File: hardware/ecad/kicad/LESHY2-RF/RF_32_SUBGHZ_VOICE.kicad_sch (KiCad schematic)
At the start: 0 parts

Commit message: complete exact H2.3.1 RF power hierarchy
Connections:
- no-connect marks 0 -> 29

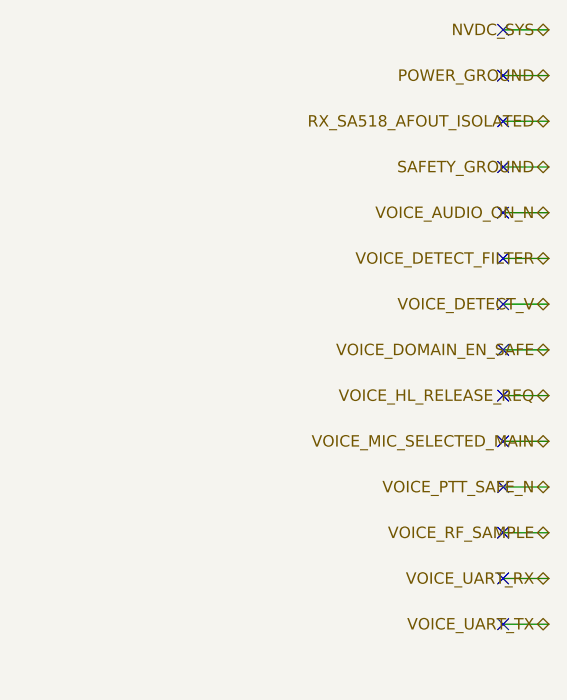
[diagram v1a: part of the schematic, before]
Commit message: complete exact H2.3.4 power rails
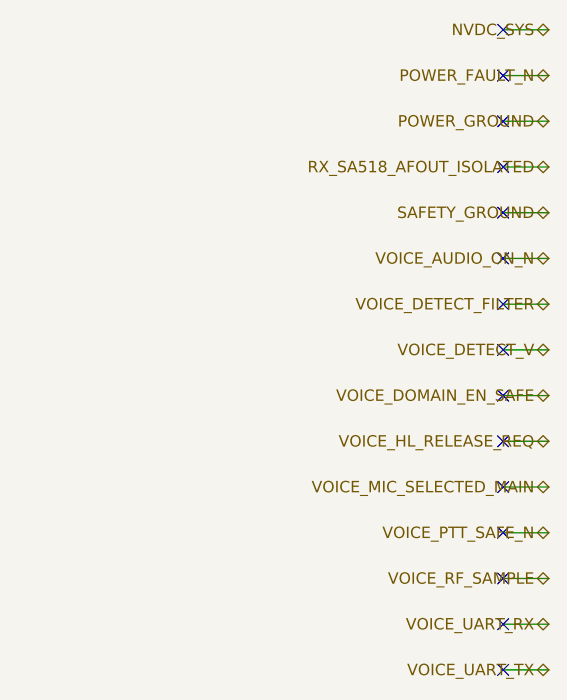
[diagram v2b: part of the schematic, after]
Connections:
- no-connect marks 29 -> 30
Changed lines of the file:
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@@
 	(no_connect (at 185.42 20.32)
 	)
-	(hierarchical_label "POWER_GROUND"
+	(hierarchical_label "POWER_FAULT_N"
 		(shape bidirectional)
 		(at 190.50 25.40 180)
@@
 	(no_connect (at 185.42 25.40)
 	)
-	(hierarchical_label "RX_SA518_AFOUT_ISOLATED"
+	(hierarchical_label "POWER_GROUND"
 		(shape bidirectional)
 		(at 190.50 30.48 180)
@@
 	(no_connect (at 185.42 30.48)
 	)
-	(hierarchical_label "SAFETY_GROUND"
+	(hierarchical_label "RX_SA518_AFOUT_ISOLATED"
 		(shape bidirectional)
 		(at 190.50 35.56 180)
@@
 	(no_connect (at 185.42 35.56)
 	)
-	(hierarchical_label "VOICE_AUDIO_ON_N"
+	(hierarchical_label "SAFETY_GROUND"
 		(shape bidirectional)
 		(at 190.50 40.64 180)
@@
 	(no_connect (at 185.42 40.64)
 	)
-	(hierarchical_label "VOICE_DETECT_FILTER"
+	(hierarchical_label "VOICE_AUDIO_ON_N"
 		(shape bidirectional)
 		(at 190.50 45.72 180)
@@
 	(no_connect (at 185.42 45.72)
 	)
-	(hierarchical_label "VOICE_DETECT_V"
+	(hierarchical_label "VOICE_DETECT_FILTER"
 		(shape bidirectional)
 		(at 190.50 50.80 180)
@@
 	(no_connect (at 185.42 50.80)
 	)
-	(hierarchical_label "VOICE_DOMAIN_EN_SAFE"
+	(hierarchical_label "VOICE_DETECT_V"
 		(shape bidirectional)
 		(at 190.50 55.88 180)
@@
 	(no_connect (at 185.42 55.88)
 	)
-	(hierarchical_label "VOICE_HL_RELEASE_REQ"
+	(hierarchical_label "VOICE_DOMAIN_EN_SAFE"
 		(shape bidirectional)
 		(at 190.50 60.96 180)
@@
 	(no_connect (at 185.42 60.96)
 	)
-	(hierarchical_label "VOICE_MIC_SELECTED_MAIN"
+	(hierarchical_label "VOICE_HL_RELEASE_REQ"
 		(shape bidirectional)
 		(at 190.50 66.04 180)
@@
 	(no_connect (at 185.42 66.04)
 	)
-	(hierarchical_label "VOICE_PTT_SAFE_N"
+	(hierarchical_label "VOICE_MIC_SELECTED_MAIN"
 		(shape bidirectional)
 		(at 190.50 71.12 180)
@@
 	(no_connect (at 185.42 71.12)
 	)
-	(hierarchical_label "VOICE_RF_SAMPLE"
+	(hierarchical_label "VOICE_PTT_SAFE_N"
 		(shape bidirectional)
 		(at 190.50 76.20 180)
@@
 	(no_connect (at 185.42 76.20)
 	)
-	(hierarchical_label "VOICE_UART_RX"
+	(hierarchical_label "VOICE_RF_SAMPLE"
 		(shape bidirectional)
 		(at 190.50 81.28 180)
@@
 	(no_connect (at 185.42 81.28)
 	)
-	(hierarchical_label "VOICE_UART_TX"
+	(hierarchical_label "VOICE_UART_RX"
 		(shape bidirectional)
 		(at 190.50 86.36 180)
@@
 	(no_connect (at 185.42 86.36)
 	)
+	(hierarchical_label "VOICE_UART_TX"
+		(shape bidirectional)
+		(at 190.50 91.44 180)
+		(effects (font (size 1.27 1.27)) (justify right))
+	)
+	(wire
+		(pts (xy 190.50 91.44) (xy 185.42 91.44))
+		(stroke (width 0) (type default))
+	)
+	(no_connect (at 185.42 91.44)
+	)
 	(sheet_instances

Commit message: complete exact H2.3.7 Sub-GHz and voice sheet
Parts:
- added C1: TDK C1005X7R1H104K050BB, Capacitor_SMD:C_0402_1005Metric, symbol Leshy2:RF32_CC_HOST_BUFFER_BYPASS
- added C10: TDK C1005X7R1H104K050BB, Capacitor_SMD:C_0402_1005Metric, symbol Leshy2:RF32_CC_AVDD15_BYPASS
- added C11: TDK C1005X7R1H104K050BB, Capacitor_SMD:C_0402_1005Metric, symbol Leshy2:RF32_CC_DCOUPL_CAP
- added C12: Murata GJM1555C1H150JB01D, Capacitor_SMD:C_0402_1005Metric, symbol Leshy2:RF32_CC_CRYSTAL_LOAD_Q1
- added C13: Murata GJM1555C1H150JB01D, Capacitor_SMD:C_0402_1005Metric, symbol Leshy2:RF32_CC_CRYSTAL_LOAD_Q2
- added C14: Murata GJM1555C1H101JB01D, Capacitor_SMD:C_0402_1005Metric, symbol Leshy2:RF32_CC_RF_P_DC_BLOCK
- added C15: Murata GJM1555C1H101JB01D, Capacitor_SMD:C_0402_1005Metric, symbol Leshy2:RF32_CC_RF_N_DC_BLOCK
- added C16: Murata GJM1555C1HR60BB01D, Capacitor_SMD:C_0402_1005Metric, symbol Leshy2:RF32_CC_RF_DIFF_CAP
- added C17: Murata GJM1555C1H1R2BB01D, Capacitor_SMD:C_0402_1005Metric, symbol Leshy2:RF32_CC_MATCH_C1P2
- added C18: Murata GJM1555C1H8R0DB01D, Capacitor_SMD:C_0402_1005Metric, symbol Leshy2:RF32_CC_315_SHUNT_C8P
- added C19: Murata GJM1555C1H100JB01D, Capacitor_SMD:C_0402_1005Metric, symbol Leshy2:RF32_CC_433_SHUNT_C10P
- added C2: TDK C1005X7R1H104K050BB, Capacitor_SMD:C_0402_1005Metric, symbol Leshy2:RF32_CC_RETURN_BUFFER_BYPASS
- added C20: Murata GJM1555C1H6R2DB01D, Capacitor_SMD:C_0402_1005Metric, symbol Leshy2:RF32_CC_433_SHUNT_C6P2
- added C21: Murata GJM1555C1HR47BB01D, Capacitor_SMD:C_0402_1005Metric, symbol Leshy2:RF32_CC_DETECTOR_TAP_CAP
- added C22: Murata GRM1555C1H121JA01D, Capacitor_SMD:C_0402_1005Metric, symbol Leshy2:RF32_CC_DETECTOR_FILTER
- added C23: TDK C1005X7R1H104K050BB, Capacitor_SMD:C_0402_1005Metric, symbol Leshy2:RF32_CC_DETECTOR_BYPASS
- added C24: Murata GRM1555C1H121JA01D, Capacitor_SMD:C_0402_1005Metric, symbol Leshy2:RF32_VOICE_DETECTOR_FILTER
- added C25: TDK C1005X7R1H104K050BB, Capacitor_SMD:C_0402_1005Metric, symbol Leshy2:RF32_VOICE_DETECTOR_BYPASS
- added C26: TDK C1608X7R1C105K080AC, Capacitor_SMD:C_0603_1608Metric, symbol Leshy2:RF32_VOICE_MIC_COUPLING
- added C27: TDK C1005X7R1H104K050BB, Capacitor_SMD:C_0402_1005Metric, symbol Leshy2:RF32_VOICE_SUPERVISOR_BYPASS
- added C28: Murata GRM155R71H103KA88D, Capacitor_SMD:C_0402_1005Metric, symbol Leshy2:RF32_VOICE_SUPERVISOR_CT
- added C29: TDK C1608X7R1C105K080AC, Capacitor_SMD:C_0603_1608Metric, symbol Leshy2:RF32_VOICE_IO_POWER_INPUT_CAP
- added C3: TDK C1005X7R1H104K050BB, Capacitor_SMD:C_0402_1005Metric, symbol Leshy2:RF32_CC_BAND_BUFFER_BYPASS
- added C30: TDK C1608X7R1C105K080AC, Capacitor_SMD:C_0603_1608Metric, symbol Leshy2:RF32_VOICE_IO_POWER_OUTPUT_CAP
- added C31: TDK C1005X7R1H104K050BB, Capacitor_SMD:C_0402_1005Metric, symbol Leshy2:RF32_VOICE_PTT_ISO_BYPASS
- added C32: TDK C1005X7R1H104K050BB, Capacitor_SMD:C_0402_1005Metric, symbol Leshy2:RF32_VOICE_UART_TX_ISO_BYPASS
- added C33: TDK C1005X7R1H104K050BB, Capacitor_SMD:C_0402_1005Metric, symbol Leshy2:RF32_VOICE_HL_DRIVER_BYPASS
- added C34: TDK C1005X7R1H104K050BB, Capacitor_SMD:C_0402_1005Metric, symbol Leshy2:RF32_VOICE_AUDIO_ISO_BYPASS
- added C35: Murata GRM32ER71E226KE15L, Capacitor_SMD:C_1210_3225Metric, symbol Leshy2:RF32_VOICE_INPUT_CAP
- added C36: TDK C1005X7R1H104K050BB, Capacitor_SMD:C_0402_1005Metric, symbol Leshy2:RF32_VOICE_HF_INPUT_CAP
- added C37: KEMET C0402C330J5GACTU, Capacitor_SMD:C_0402_1005Metric, symbol Leshy2:RF32_VOICE_FF_CAP
- added C38: Murata GRM32ER71E226KE15L, Capacitor_SMD:C_1210_3225Metric, symbol Leshy2:RF32_VOICE_OUTPUT_CAP0
- added C39: Murata GRM32ER71E226KE15L, Capacitor_SMD:C_1210_3225Metric, symbol Leshy2:RF32_VOICE_OUTPUT_CAP1
- added C4: TDK C1608X7R1C105K080AC, Capacitor_SMD:C_0603_1608Metric, symbol Leshy2:RF32_CC_POWER_INPUT_CAP
- added C40: Murata GRM155R71H472KA01D, Capacitor_SMD:C_0402_1005Metric, symbol Leshy2:RF32_VOICE_EFUSE_DVDT_CAP
- added C41: Murata GRM1555C1H121JA01D, Capacitor_SMD:C_0402_1005Metric, symbol Leshy2:RF32_VOICE_EFUSE_ITIMER_CAP
- added C42: Murata GRM188R60J106ME47D, Capacitor_SMD:C_0603_1608Metric, symbol Leshy2:RF32_VOICE_EFUSE_OUTPUT_CAP
- added C5: TDK C1608X7R1C105K080AC, Capacitor_SMD:C_0603_1608Metric, symbol Leshy2:RF32_CC_LOCAL_BULK_CAP
- added C6: TDK C1005X7R1H104K050BB, Capacitor_SMD:C_0402_1005Metric, symbol Leshy2:RF32_CC_DVDD_BYPASS
- added C7: TDK C1005X7R1H104K050BB, Capacitor_SMD:C_0402_1005Metric, symbol Leshy2:RF32_CC_AVDD9_BYPASS
- added C8: TDK C1005X7R1H104K050BB, Capacitor_SMD:C_0402_1005Metric, symbol Leshy2:RF32_CC_AVDD11_BYPASS
- added C9: TDK C1005X7R1H104K050BB, Capacitor_SMD:C_0402_1005Metric, symbol Leshy2:RF32_CC_AVDD14_BYPASS
- added D1: Littelfuse SESD0402X1UN-0020-090, Diode_SMD:D_0402_1005Metric, symbol Leshy2:RF32_CC_RF_ESD
- added D2: Nexperia PESD24VY1BSF, Diode_SMD:Nexperia_DSN0603-2_0.6x0.3mm_P0.4mm, symbol Leshy2:RF32_VOICE_RF_ESD
- added J1: GCT RFPC-SMA31-FN-175-A, Leshy2:RFPC-SMA31-FN-175-A, symbol Leshy2:RF32_CC_EXTERNAL_SMA
- added J2: GCT RFPC-SMA31-FN-175-A, Leshy2:RFPC-SMA31-FN-175-A, symbol Leshy2:RF32_VOICE_EXTERNAL_SMA
- added L1: Murata LQG15HS3N3S02D, Inductor_SMD:L_0402_1005Metric, symbol Leshy2:RF32_CC_MATCH_L3N3
- added L2: Murata LQG15HS6N8J02D, Inductor_SMD:L_0402_1005Metric, symbol Leshy2:RF32_CC_MATCH_L6N8
- added L3: Murata LQG15HS10NJ02D, Inductor_SMD:L_0402_1005Metric, symbol Leshy2:RF32_CC_315_L10_IN
- added L4: Murata LQG15HS3N6S02D, Inductor_SMD:L_0402_1005Metric, symbol Leshy2:RF32_CC_315_SHUNT_L3N6
- added L5: Murata LQG15HS10NJ02D, Inductor_SMD:L_0402_1005Metric, symbol Leshy2:RF32_CC_315_L10_OUT
- added L6: Murata LQG15HS15NJ02D, Inductor_SMD:L_0402_1005Metric, symbol Leshy2:RF32_CC_433_L15
- added L7: Murata LQG15HS10NJ02D, Inductor_SMD:L_0402_1005Metric, symbol Leshy2:RF32_CC_868_915_L10
- added L8: Murata LQG15HS2N2S02D, Inductor_SMD:L_0402_1005Metric, symbol Leshy2:RF32_CC_OUTPUT_L2N2
- added L9: Sunlord MWSA0503S-3R3MT, Inductor_SMD:L_Sunlord_MWSA0503S, symbol Leshy2:RF32_VOICE_INDUCTOR
- added Q1: Diodes Incorporated MMBT3904-7-F, Package_TO_SOT_SMD:SOT-23, symbol Leshy2:RF32_VOICE_PG_QUALIFIER
- added R1: Yageo RC0402FR-0710KL, Resistor_SMD:R_0402_1005Metric, symbol Leshy2:RF32_CC_POWER_ON_PULLDOWN
- added R10: Panasonic ERJ-2RKF22R0X, Resistor_SMD:R_0402_1005Metric, symbol Leshy2:RF32_CC_BAND_V2_SERIES
- added R11: Yageo RC0402FR-0710KL, Resistor_SMD:R_0402_1005Metric, symbol Leshy2:RF32_CC_HOST_SCLK_PULLDOWN
- added R12: Yageo RC0402FR-0710KL, Resistor_SMD:R_0402_1005Metric, symbol Leshy2:RF32_CC_HOST_SI_PULLDOWN
- added R13: Yageo RC0402FR-0710KL, Resistor_SMD:R_0402_1005Metric, symbol Leshy2:RF32_CC_HOST_CSN_PULLUP
- added R14: Yageo RC0402FR-0710KL, Resistor_SMD:R_0402_1005Metric, symbol Leshy2:RF32_CC_HOST_SO_PULLDOWN
- added R15: Yageo RC0402FR-0710KL, Resistor_SMD:R_0402_1005Metric, symbol Leshy2:RF32_CC_HOST_GDO0_PULLDOWN
- added R16: Yageo RC0402FR-0710KL, Resistor_SMD:R_0402_1005Metric, symbol Leshy2:RF32_CC_HOST_GDO2_PULLDOWN
- added R17: Yageo RC0402FR-0710KL, Resistor_SMD:R_0402_1005Metric, symbol Leshy2:RF32_CC_BAND_V1_HOST_PULLDOWN
- added R18: Yageo RC0402FR-0710KL, Resistor_SMD:R_0402_1005Metric, symbol Leshy2:RF32_CC_BAND_V2_HOST_PULLDOWN
- added R19: Yageo RC0402FR-0710KL, Resistor_SMD:R_0402_1005Metric, symbol Leshy2:RF32_CC_SWITCH_A_V1_PULLDOWN
- added R2: Yageo RC0402FR-0756KL, Resistor_SMD:R_0402_1005Metric, symbol Leshy2:RF32_CC_RBIAS_RES
- added R20: Yageo RC0402FR-0710KL, Resistor_SMD:R_0402_1005Metric, symbol Leshy2:RF32_CC_SWITCH_A_V2_PULLDOWN
- added R21: Yageo RC0402FR-0710KL, Resistor_SMD:R_0402_1005Metric, symbol Leshy2:RF32_CC_SWITCH_B_V1_PULLDOWN
- added R22: Yageo RC0402FR-0710KL, Resistor_SMD:R_0402_1005Metric, symbol Leshy2:RF32_CC_SWITCH_B_V2_PULLDOWN
- added R23: Yageo RC0402FR-075K1L, Resistor_SMD:R_0402_1005Metric, symbol Leshy2:RF32_VOICE_DETECTOR_SERIES_ATTENUATOR
- added R24: Yageo RC0402FR-0752R3L, Resistor_SMD:R_0402_1005Metric, symbol Leshy2:RF32_VOICE_DETECTOR_MATCH
- added R25: Yageo RC0402FR-0747KL, Resistor_SMD:R_0402_1005Metric, symbol Leshy2:RF32_VOICE_SUPERVISOR_SENSE_TOP
- added R26: Yageo RC0402FR-07220KL, Resistor_SMD:R_0402_1005Metric, symbol Leshy2:RF32_VOICE_SUPERVISOR_SENSE_BOTTOM
- added R27: Yageo RC0402FR-0710KL, Resistor_SMD:R_0402_1005Metric, symbol Leshy2:RF32_VOICE_SUPERVISOR_PULLUP
- added R28: Yageo RC0402FR-0710KL, Resistor_SMD:R_0402_1005Metric, symbol Leshy2:RF32_VOICE_PTT_PULLUP
- added R29: Yageo RC0402FR-07100KL, Resistor_SMD:R_0402_1005Metric, symbol Leshy2:RF32_VOICE_UART_RX_PULLDOWN
- added R3: Panasonic ERJ-2RKF22R0X, Resistor_SMD:R_0402_1005Metric, symbol Leshy2:RF32_CC_SCLK_SERIES
- added R30: Yageo RC0402FR-07100KL, Resistor_SMD:R_0402_1005Metric, symbol Leshy2:RF32_VOICE_UART_TX_PULLDOWN
- added R31: Yageo RC0402FR-0710KL, Resistor_SMD:R_0402_1005Metric, symbol Leshy2:RF32_VOICE_HL_REQ_PULLDOWN
- added R32: Yageo RC0402FR-07100KL, Resistor_SMD:R_0402_1005Metric, symbol Leshy2:RF32_VOICE_AUDIO_ON_PULLDOWN
- added R33: Yageo RC0402FR-0768KL, Resistor_SMD:R_0402_1005Metric, symbol Leshy2:RF32_VOICE_FB_TOP
- added R34: Yageo RC0402FR-0712KL, Resistor_SMD:R_0402_1005Metric, symbol Leshy2:RF32_VOICE_FB_BOTTOM
- added R35: Yageo RC0402FR-073K32L, Resistor_SMD:R_0402_1005Metric, symbol Leshy2:RF32_VOICE_EFUSE_RILM
- added R36: Yageo RC0402FR-07270KL, Resistor_SMD:R_0402_1005Metric, symbol Leshy2:RF32_VOICE_EFUSE_OVLO_TOP
- added R37: Yageo RC0402FR-07100KL, Resistor_SMD:R_0402_1005Metric, symbol Leshy2:RF32_VOICE_EFUSE_OVLO_BOTTOM
- added R38: Yageo RC0402FR-0768KL, Resistor_SMD:R_0402_1005Metric, symbol Leshy2:RF32_VOICE_EFUSE_PG_TOP
- added R39: Yageo RC0402FR-0733KL, Resistor_SMD:R_0402_1005Metric, symbol Leshy2:RF32_VOICE_EFUSE_PG_BOTTOM
- added R4: Panasonic ERJ-2RKF22R0X, Resistor_SMD:R_0402_1005Metric, symbol Leshy2:RF32_CC_SI_SERIES
- added R40: Yageo RC0402FR-0710KL, Resistor_SMD:R_0402_1005Metric, symbol Leshy2:RF32_VOICE_EN_PULLDOWN
- added R41: Yageo RC0402FR-0710KL, Resistor_SMD:R_0402_1005Metric, symbol Leshy2:RF32_VOICE_PG_PULLUP
- added R42: Yageo RC0402FR-0768KL, Resistor_SMD:R_0402_1005Metric, symbol Leshy2:RF32_VOICE_PG_BASE_RES
- added R5: Panasonic ERJ-2RKF22R0X, Resistor_SMD:R_0402_1005Metric, symbol Leshy2:RF32_CC_CSN_SERIES
- added R6: Panasonic ERJ-2RKF22R0X, Resistor_SMD:R_0402_1005Metric, symbol Leshy2:RF32_CC_SO_SERIES
- added R7: Panasonic ERJ-2RKF22R0X, Resistor_SMD:R_0402_1005Metric, symbol Leshy2:RF32_CC_GDO0_SERIES
- added R8: Panasonic ERJ-2RKF22R0X, Resistor_SMD:R_0402_1005Metric, symbol Leshy2:RF32_CC_GDO2_SERIES
- added R9: Panasonic ERJ-2RKF22R0X, Resistor_SMD:R_0402_1005Metric, symbol Leshy2:RF32_CC_BAND_V1_SERIES
- added U1: CC1101RGPR, Package_DFN_QFN:Texas_RGP0020D_VQFN-20-1EP_4x4mm_P0.5mm_EP2.7x2.7mm, symbol Leshy2:RF32_CC
- added U10: Texas Instruments TPS22919DCKR, Package_TO_SOT_SMD:SOT-363_SC-70-6, symbol Leshy2:RF32_VOICE_IO_POWER_SWITCH
- added U11: Texas Instruments SN74LVC1G126DCKR, Package_TO_SOT_SMD:Texas_R-PDSO-G5_DCK-5, symbol Leshy2:RF32_VOICE_PTT_ISO
- added U12: Texas Instruments SN74LVC1G126DCKR, Package_TO_SOT_SMD:Texas_R-PDSO-G5_DCK-5, symbol Leshy2:RF32_VOICE_UART_TX_ISO
- added U13: SN74LVC1G07DCKR, Package_TO_SOT_SMD:Texas_R-PDSO-G5_DCK-5, symbol Leshy2:RF32_VOICE_HL_DRIVER
- added U14: Texas Instruments SN74LVC2G66DCUR, Package_SO:VSSOP-8_2.3x2mm_P0.5mm, symbol Leshy2:RF32_VOICE_AUDIO_ISO
- added U15: Texas Instruments TPS564252DRLR, Package_TO_SOT_SMD:Texas_R-PDSO-N6_DRL-6, symbol Leshy2:RF32_VOICE_BUCK
- added U16: Texas Instruments TPS25974LRPWR, Leshy2:TI-RPW0010A-VQFN-HR-10, symbol Leshy2:RF32_VOICE_EFUSE
- added U17: Texas Instruments TPS22919DCKR, Package_TO_SOT_SMD:SOT-363_SC-70-6, symbol Leshy2:RF32_CC_POWER_SWITCH
- added U2: Nexperia 74LVC126APW,118, Package_SO:TSSOP-14_4.4x5mm_P0.65mm, symbol Leshy2:RF32_CC_HOST_BUFFER
- added U3: Nexperia 74LVC126APW,118, Package_SO:TSSOP-14_4.4x5mm_P0.65mm, symbol Leshy2:RF32_CC_RETURN_BUFFER
- added U4: Nexperia 74LVC2G126DC,125, Package_SO:VSSOP-8_2.3x2mm_P0.5mm, symbol Leshy2:RF32_CC_BAND_BUFFER
- added U5: TTM Technologies B0310J50100AHF, Leshy2:B0310J50100AHF, symbol Leshy2:RF32_CC_BALUN
- added U6: Infineon BGS13SN8E6327XTSA1, Leshy2:Infineon-PG-TSNP-8-1, symbol Leshy2:RF32_CC_SWITCH_A
- added U7: Infineon BGS13SN8E6327XTSA1, Leshy2:Infineon-PG-TSNP-8-1, symbol Leshy2:RF32_CC_SWITCH_B
- added U8: NiceRF SA518, Leshy2:NiceRF-SA518-Rev1.1-H5-CONTACT-AXIS-RESERVE, symbol Leshy2:RF32_VOICE
- added U9: TPS3808G33DBVR, Package_TO_SOT_SMD:SOT-23-6, symbol Leshy2:RF32_VOICE_SUPERVISOR
- added Y1: Abracon ABM8-26.000MHZ-10-D-1-G-T, Crystal:Crystal_SMD_Abracon_ABM8G-4Pin_3.2x2.5mm, symbol Leshy2:RF32_CC_CRYSTAL
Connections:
- net 3V3_MAIN: now also C29.1 (END_1), C33.1 (END_1), C4.1 (END_1), R13.2 (END_2), R41.1 (END_1), U10.1 (IN), U13.5 (VCC), U17.1 (IN)
- net AON_SAFE_3V3: now also C23.1 (END_1), C25.1 (END_1), C27.1 (END_1), R27.1 (END_1), U9.6 (VDD)
- net AUDIO_GROUND: now also C30.2 (END_2), C31.2 (END_2), C32.2 (END_2), C34.2 (END_2), R29.2 (END_2), U11.3 (GND), U12.3 (GND), U14.4 (GND)
- net CC_BAND_V1_REQ: now also R17.1 (END_1), U4.2 (1A)
- net CC_BAND_V2_REQ: now also R18.1 (END_1), U4.5 (2A)
- net CC_CSN_N: now also R13.1 (END_1), U2.9 (3A)
- net CC_DETECT_FILTER: now also C22.1 (END_1)
- net CC_DETECT_V: now also C22.2 (END_2)
- net CC_GDO0: now also R15.1 (END_1), R7.2 (END_2)
- net CC_GDO2: now also R16.1 (END_1), R8.2 (END_2)
- net CC_MISO: now also R14.1 (END_1), R6.2 (END_2)
- net CC_MOSI: now also R12.1 (END_1), U2.5 (2A)
- net CC_PWR_EN_SAFE: now also R1.1 (END_1), U17.3 (ON)
- net CC_RF_SAMPLE: now also C21.2 (END_2)
- net CC_SCK: now also R11.1 (END_1), U2.2 (1A)
- net NVDC_SYS: now also C35.1 (END_1), C36.1 (END_1), U15.1 (VIN)
- net POWER_FAULT_N: now also Q1.3 (C)
- net POWER_GROUND: now also C1.2 (END_2), C10.2 (END_2), C11.2 (END_2), C12.2 (END_2), C13.2 (END_2), C17.2 (END_2), C18.2 (END_2), C19.2 (END_2), C2.2 (END_2), C20.2 (END_2), C29.2 (END_2), C3.2 (END_2), C33.2 (END_2), C35.2 (END_2), C36.2 (END_2), C38.2 (END_2), C39.2 (END_2), C4.2 (END_2), C40.2 (END_2), C41.2 (END_2), C42.2 (END_2), C5.2 (END_2), C6.2 (END_2), C7.2 (END_2), C8.2 (END_2), C9.2 (END_2), D1.2 (A), D2.2 (K2), J1.2 (GROUND_TOP_LEFT), J1.3 (GROUND_TOP_RIGHT), J1.4 (GROUND_BOTTOM_LEFT), J1.5 (GROUND_BOTTOM_RIGHT), J2.2 (GROUND_TOP_LEFT), J2.3 (GROUND_TOP_RIGHT), J2.4 (GROUND_BOTTOM_LEFT), J2.5 (GROUND_BOTTOM_RIGHT), R1.2 (END_2), R11.2 (END_2), R12.2 (END_2), R14.2 (END_2), R15.2 (END_2), R16.2 (END_2), R17.2 (END_2), R18.2 (END_2), R19.2 (END_2), R2.2 (END_2), R20.2 (END_2), R21.2 (END_2), R22.2 (END_2), R24.2 (END_2), R30.2 (END_2), R31.2 (END_2), R32.2 (END_2), R34.2 (END_2), R35.2 (END_2), R37.2 (END_2), R39.2 (END_2), R40.2 (END_2), U1.16 (GND_16), U1.18 (DGUARD), U1.19 (GND_19), U1.21 (EPAD), U10.2 (GND), U13.3 (GND), U15.3 (GND), U16.8 (GND), U17.2 (GND), U2.12 (4A), U2.13 (4OE), U2.7 (GND), U3.12 (4A), U3.13 (4OE), U3.7 (GND), U4.4 (GND), U5.2 (GND), U6.8 (GND), U7.8 (GND), U8.10 (GND_10), U8.19 (GND_19), U8.20 (GND_20), U8.8 (GND_8), U8.9 (GND_9), Y1.2 (GND_2), Y1.4 (GND_4)
- net RX_SA518_AFOUT_ISOLATED: now also U14.2 (1B)
- net SAFETY_GROUND: now also C23.2 (END_2), C25.2 (END_2), C27.2 (END_2), C28.2 (END_2), R26.2 (END_2), U9.2 (GND)
- net VOICE_AUDIO_ON_N: now also R32.1 (END_1), U8.18 (AUDIO_ON)
- net VOICE_DETECT_FILTER: now also C24.1 (END_1)
- net VOICE_DETECT_V: now also C24.2 (END_2)
- net VOICE_DOMAIN_EN_SAFE: now also R40.1 (END_1), R42.1 (END_1), U15.5 (EN), U9.3 (MR_N)
- net VOICE_HL_RELEASE_REQ: now also R31.1 (END_1), U13.2 (A)
- net VOICE_MIC_SELECTED_MAIN: now also U14.5 (2A)
- net VOICE_PTT_SAFE_N: now also U11.2 (A)
- net VOICE_RF_SAMPLE: now also R23.2 (END_2), R24.1 (END_1)
- net VOICE_UART_RX: now also R30.1 (END_1), U8.2 (UART_TX)
- net VOICE_UART_TX: now also U12.2 (A)
- new net 3V3_CC_SWITCHED: C1.1 (END_1), C10.1 (END_1), C2.1 (END_1), C3.1 (END_1), C5.1 (END_1), C6.1 (END_1), C7.1 (END_1), C8.1 (END_1), C9.1 (END_1), U1.11 (AVDD_11), U1.14 (AVDD_14), U1.15 (AVDD_15), U1.4 (DVDD), U1.9 (AVDD_9), U17.5 (QOD), U17.6 (VOUT), U2.1 (1OE), U2.10 (3OE), U2.14 (VCC), U2.4 (2OE), U3.1 (1OE), U3.10 (3OE), U3.14 (VCC), U3.4 (2OE), U4.1 (1OE), U4.7 (2OE), U4.8 (VCC), U6.1 (VDD), U7.1 (VDD)
- new net CC_BAND_V1: R19.1 (END_1), R21.1 (END_1), R9.2 (END_2), U6.3 (V1), U7.3 (V1)
- new net CC_BAND_V1_BUFFERED: R9.1 (END_1), U4.6 (1Y)
- new net CC_BAND_V2: R10.2 (END_2), R20.1 (END_1), R22.1 (END_1), U6.2 (V2), U7.2 (V2)
- new net CC_BAND_V2_BUFFERED: R10.1 (END_1), U4.3 (2Y)
- new net CC_CSN_BUFFERED_N: R5.1 (END_1), U2.8 (3Y)
- new net CC_CSN_DEVICE_N: R5.2 (END_2), U1.7 (CSN)
- new net CC_DCOUPL: C11.1 (END_1), U1.5 (DCOUPL)
- new net CC_EXTERNAL_RF_50R: C21.1 (END_1), D1.1 (K), J1.1 (RF), L8.2 (END_2)
- new net CC_GDO0_BUFFERED: R7.1 (END_1), U3.6 (2Y)
- new net CC_GDO0_DEVICE: U1.6 (GDO0), U3.5 (2A)
- new net CC_GDO2_BUFFERED: R8.1 (END_1), U3.8 (3Y)
- new net CC_GDO2_DEVICE: U1.3 (GDO2), U3.9 (3A)
- new net CC_RBIAS: R2.1 (END_1), U1.17 (RBIAS)
- new net CC_RF_315_IN: L3.1 (END_1), U6.5 (RF1)
- new net CC_RF_315_MID: L3.2 (END_2), L4.1 (END_1), L5.1 (END_1)
- new net CC_RF_315_OUT: L5.2 (END_2), U7.5 (RF1)
- new net CC_RF_315_TRAP: C18.1 (END_1), L4.2 (END_2)
- new net CC_RF_433_IN: C19.1 (END_1), L6.1 (END_1), U6.7 (RF2)
- new net CC_RF_433_OUT: C20.1 (END_1), L6.2 (END_2), U7.7 (RF2)
- new net CC_RF_868_915_IN: L7.1 (END_1), U6.4 (RF3)
- new net CC_RF_868_915_OUT: L7.2 (END_2), U7.4 (RF3)
- new net CC_RF_BAL_A: C14.2 (END_2), C16.1 (END_1), U5.3 (BALANCED_A)
- new net CC_RF_BAL_B: C15.2 (END_2), C16.2 (END_2), U5.4 (BALANCED_B)
- new net CC_RF_MATCH_MID: C17.1 (END_1), L1.2 (END_2), L2.1 (END_1)
- new net CC_RF_N: C15.1 (END_1), U1.13 (RF_N)
- new net CC_RF_P: C14.1 (END_1), U1.12 (RF_P)
- new net CC_RF_SELECTED: L8.1 (END_1), U7.6 (RFIN)
- new net CC_RF_SWITCH_INPUT: L2.2 (END_2), U6.6 (RFIN)
- new net CC_RF_UNBALANCED: L1.1 (END_1), U5.1 (UNBALANCED)
- new net CC_SCLK_BUFFERED: R3.1 (END_1), U2.3 (1Y)
- new net CC_SCLK_DEVICE: R3.2 (END_2), U1.1 (SCLK)
- new net CC_SI_BUFFERED: R4.1 (END_1), U2.6 (2Y)
- new net CC_SI_DEVICE: R4.2 (END_2), U1.20 (SI)
- new net CC_SO_BUFFERED: R6.1 (END_1), U3.3 (1Y)
- new net CC_SO_DEVICE: U1.2 (SO_GDO1), U3.2 (1A)
- new net CC_XOSC_Q1: C12.1 (END_1), U1.8 (XOSC_Q1), Y1.1 (X1)
- new net CC_XOSC_Q2: C13.1 (END_1), U1.10 (XOSC_Q2), Y1.3 (X2)
- new net RX_SA518_AFOUT_LOCAL: U14.1 (1A), U8.16 (AFOUT)
- new net VOICE_4V_FB: C37.2 (END_2), R33.2 (END_2), R34.1 (END_1), U15.6 (FB)
- new net VOICE_4V_PG_N: Q1.2 (E), R41.2 (END_2), U16.3 (PG)
- new net VOICE_4V_SENSE: R25.2 (END_2), R26.1 (END_1), U9.5 (SENSE)
- new net VOICE_BUCK_SW: L9.1 (END_1), U15.2 (SW)
- new net VOICE_EFUSE_DVDT: C40.1 (END_1), U16.7 (DVDT)
- new net VOICE_EFUSE_ILM: R35.1 (END_1), U16.9 (ILM)
- new net VOICE_EFUSE_ITIMER: C41.1 (END_1), U16.10 (ITIMER)
- new net VOICE_EFUSE_OVLO: R36.2 (END_2), R37.1 (END_1), U16.2 (OVLO)
- new net VOICE_EFUSE_PGTH: R38.2 (END_2), R39.1 (END_1), U16.4 (PGTH)
- new net VOICE_EXTERNAL_RF_50R: D2.1 (K1), J2.1 (RF), R23.1 (END_1), U8.7 (ANT)
- new net VOICE_HL_OPEN_DRAIN: U13.4 (Y), U8.12 (HL)
- new net VOICE_MIC_IN: C26.2 (END_2), U8.1 (MIC_IN)
- new net VOICE_MIC_SELECTED_ISOLATED: C26.1 (END_1), U14.6 (2B)
- new net VOICE_PG_QUAL_BASE: Q1.1 (B), R42.2 (END_2)
- new net VOICE_PTT_MODULE_N: R28.2 (END_2), U11.4 (Y), U8.14 (PTT)
- new net VOICE_RAW_4V_PG_N: U15.4 (PG)
- new net VOICE_READY: R27.2 (END_2), U10.3 (ON), U11.1 (OE), U12.1 (OE), U14.3 (2C), U14.7 (1C), U8.13 (PD), U9.1 (RESET_N)
- new net VOICE_READY_DELAY: C28.1 (END_1), U9.4 (CT)
- new net VOICE_UART_RX_MODULE: R29.1 (END_1), U12.4 (Y), U8.3 (UART_RX)
- new net VOICE_UPDATE_FIXTURE: U8.17 (UPDATE)
- new net VVOICE_4V: C42.1 (END_1), R25.1 (END_1), R38.1 (END_1), U16.6 (OUT), U8.11 (VCC)
- new net VVOICE_IO_3V3: C30.1 (END_1), C31.1 (END_1), C32.1 (END_1), C34.1 (END_1), R28.1 (END_1), U10.5 (QOD), U10.6 (VOUT), U11.5 (VCC), U12.5 (VCC), U14.8 (VCC)
- new net VVOICE_RAW_4V: C37.1 (END_1), C38.1 (END_1), C39.1 (END_1), L9.2 (END_2), R33.1 (END_1), R36.1 (END_1), U16.1 (EN_UVLO), U16.5 (IN)
- no-connect marks 30 -> 11
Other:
- title: (none) -> Leshy2 — independent CC1101 Sub-GHz data and SA518 voice

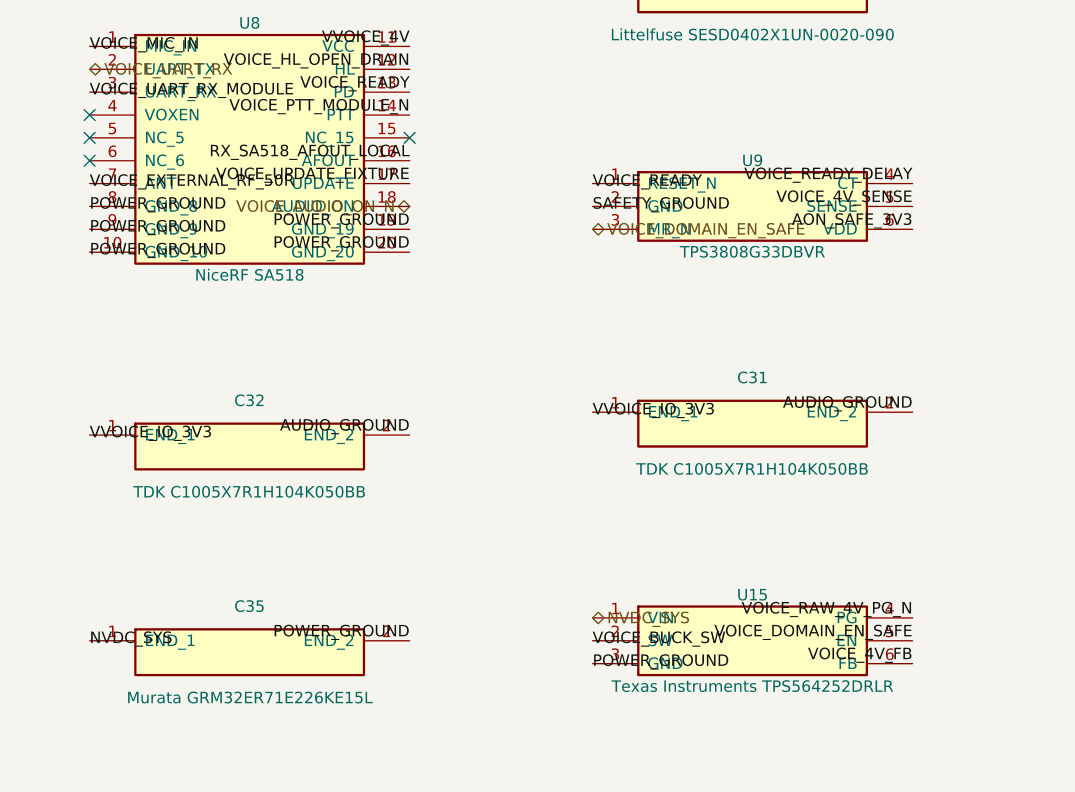
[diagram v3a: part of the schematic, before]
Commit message: complete exact H2.3.13 RF testpoint sheet
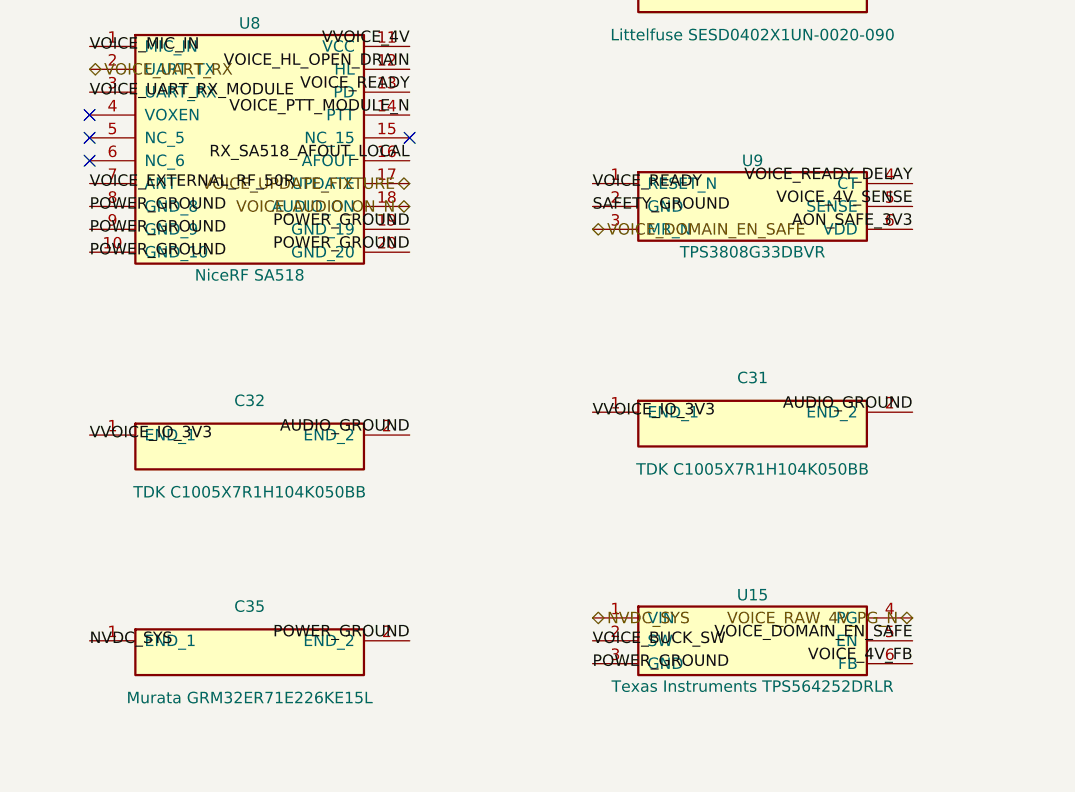
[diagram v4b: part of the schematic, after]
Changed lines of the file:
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@@
 		(effects (font (size 1.27 1.27)))
 	)
-	(label "VOICE_RAW_4V_PG_N"
+	(hierarchical_label "VOICE_RAW_4V_PG_N"
+		(shape bidirectional)
 		(at 337.82 228.60 180)
 		(effects (font (size 1.27 1.27)) (justify right bottom))
@@
 		(effects (font (size 1.27 1.27)))
 	)
-	(label "VOICE_UPDATE_FIXTURE"
+	(hierarchical_label "VOICE_UPDATE_FIXTURE"
+		(shape bidirectional)
 		(at 281.94 180.34 180)
 		(effects (font (size 1.27 1.27)) (justify right bottom))

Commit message: complete H2 schematic review package
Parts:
- renumbered C1 to C32001, C2 to C32002, C3 to C32003, C4 to C32004, C5 to C32005, C6 to C32006, C7 to C32007, C8 to C32008, C9 to C32009, C10 to C32010, C11 to C32011, C12 to C32012, C13 to C32013, C14 to C32014, C15 to C32015, C16 to C32016, C17 to C32017, C18 to C32018, C19 to C32019, C20 to C32020, C21 to C32021, C22 to C32022, C23 to C32023, C24 to C32024, C25 to C32025, C26 to C32026, C27 to C32027, C28 to C32028, C29 to C32029, C30 to C32030, C31 to C32031, C32 to C32032, C33 to C32033, C34 to C32034, C35 to C32035, C36 to C32036, C37 to C32037, C38 to C32038, C39 to C32039, C40 to C32040, C41 to C32041, C42 to C32042, D1 to D32001, D2 to D32002, J1 to J32001, J2 to J32002, L1 to L32001, L2 to L32002, L3 to L32003, L4 to L32004, L5 to L32005, L6 to L32006, L7 to L32007, L8 to L32008, L9 to L32009, Q1 to Q32001, R1 to R32001, R2 to R32002, R3 to R32003, R4 to R32004, R5 to R32005, R6 to R32006, R7 to R32007, R8 to R32008, R9 to R32009, R10 to R32010, R11 to R32011, R12 to R32012, R13 to R32013, R14 to R32014, R15 to R32015, R16 to R32016, R17 to R32017, R18 to R32018, R19 to R32019, R20 to R32020, R21 to R32021, R22 to R32022, R23 to R32023, R24 to R32024, R25 to R32025, R26 to R32026, R27 to R32027, R28 to R32028, R29 to R32029, R30 to R32030, R31 to R32031, R32 to R32032, R33 to R32033, R34 to R32034, R35 to R32035, R36 to R32036, R37 to R32037, R38 to R32038, R39 to R32039, R40 to R32040, R41 to R32041, R42 to R32042, U1 to U32001, U2 to U32002, U3 to U32003, U4 to U32004, U5 to U32005, U6 to U32006, U7 to U32007, U8 to U32008, U9 to U32009, U10 to U32010, U11 to U32011, U12 to U32012, U13 to U32013, U14 to U32014, U15 to U32015, U16 to U32016, U17 to U32017, Y1 to Y32001

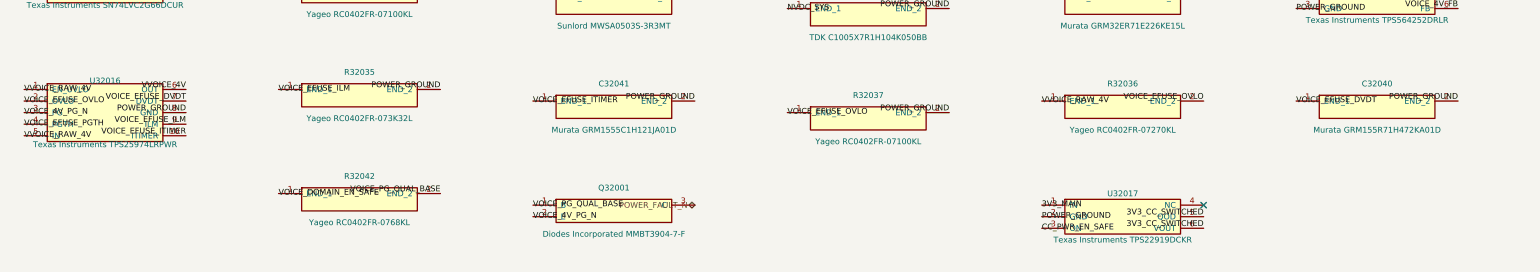
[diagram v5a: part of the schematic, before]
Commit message: review H3.6.2 single-fault containment
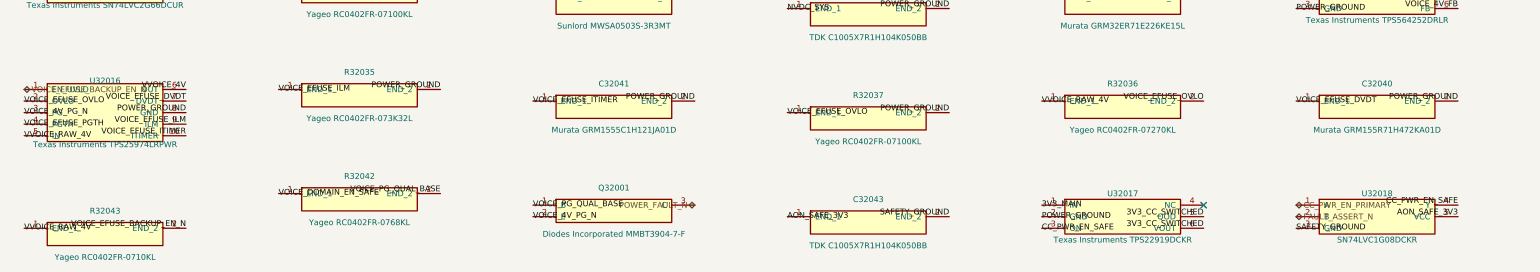
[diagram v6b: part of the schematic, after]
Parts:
- added C32043: TDK C1005X7R1H104K050BB, Capacitor_SMD:C_0402_1005Metric, symbol Leshy2:RF32_CC_BACKUP_GATE_BYPASS
- added R32043: Yageo RC0402FR-0710KL, Resistor_SMD:R_0402_1005Metric, symbol Leshy2:RF32_VOICE_EFUSE_EN_PULLUP
- added U32018: SN74LVC1G08DCKR, Package_TO_SOT_SMD:SOT-353_SC-70-5, symbol Leshy2:RF32_CC_BACKUP_GATE
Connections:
- net AON_SAFE_3V3: now also C32043.1 (END_1), U32018.5 (VCC)
- net CC_PWR_EN_SAFE: now also U32018.4 (Y)
- net SAFETY_GROUND: now also C32043.2 (END_2), U32018.3 (GND)
- net VVOICE_RAW_4V: now also R32043.1 (END_1); no longer U32016.1 (EN_UVLO)
- new net CC_PWR_EN_PRIMARY: U32018.1 (A)
- new net FAULT_ASSERT_N: U32018.2 (B)
- new net VOICE_EFUSE_BACKUP_EN_N: R32043.2 (END_2), U32016.1 (EN_UVLO)
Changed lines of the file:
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@@
+		)
+	)
+	(symbol
+		(lib_id "Leshy2:RF32_CC_BACKUP_GATE")
+		(at 320.04 279.40 0)
+		(unit 1)
+		(exclude_from_sim no)
+		(in_bom yes)
+		(on_board yes)
+		(dnp no)
+		(property "Reference" "U32018"
+			(at 320.04 274.32 0)
+			(show_name no)
+			(do_not_autoplace no)
+			(effects (font (size 1.27 1.27)))
+		)
+		(property "Value" "SN74LVC1G08DCKR"
+			(at 320.04 284.48 0)
+			(show_name no)
+			(do_not_autoplace no)
+			(effects (font (size 1.27 1.27)))
+		)
+		(property "Footprint" "Package_TO_SOT_SMD:SOT-353_SC-70-5"
+			(at 320.04 279.40 0)
+			(show_name no)
+			(do_not_autoplace no)
+			(hide yes)
+			(effects (font (size 1.27 1.27)))
+		)
+		(property "Datasheet" "~"
+			(at 320.04 279.40 0)
+			(show_name no)
+			(do_not_autoplace no)
+			(hide yes)
+			(effects (font (size 1.27 1.27)))
+		)
+		(property "Description" "independent FAULT_ASSERT_N CC1101 rail qualifier"
+			(at 320.04 279.40 0)
+			(show_name no)
+			(do_not_autoplace no)
+			(hide yes)
+			(effects (font (size 1.27 1.27)))
+		)
+		(pin "1"
+		)
+		(pin "2"
+		)
+		(pin "3"
+		)
+		(pin "4"
+		)
+		(pin "5"
+		)
+		(instances
+			(project "LESHY2-RF"
+				(path "/58797fc0-4d05-5b8c-a153-b01d4ba46651"
+					(reference "U32018")
+					(unit 1)
+				)
+			)
+		)
+	)
+	(symbol
+		(lib_id "Leshy2:RF32_CC_BACKUP_GATE_BYPASS")
+		(at 208.28 280.67 0)
+		(unit 1)
+		(exclude_from_sim no)
+		(in_bom yes)
+		(on_board yes)
+		(dnp no)
+		(property "Reference" "C32043"
+			(at 208.28 275.59 0)
+			(show_name no)
+			(do_not_autoplace no)
+			(effects (font (size 1.27 1.27)))
+		)
+		(property "Value" "TDK C1005X7R1H104K050BB"
+			(at 208.28 285.75 0)
+			(show_name no)
+			(do_not_autoplace no)
+			(effects (font (size 1.27 1.27)))
+		)
+		(property "Footprint" "Capacitor_SMD:C_0402_1005Metric"
+			(at 208.28 280.67 0)
+			(show_name no)
+			(do_not_autoplace no)
+			(hide yes)
+			(effects (font (size 1.27 1.27)))
+		)
+		(property "Datasheet" "~"
+			(at 208.28 280.67 0)
+			(show_name no)
+			(do_not_autoplace no)
+			(hide yes)
+			(effects (font (size 1.27 1.27)))
+		)
+		(property "Description" "100nf_10pct_50v_x7r_0402_converter_hf_input_capacitor"
+			(at 208.28 280.67 0)
+			(show_name no)
+			(do_not_autoplace no)
+			(hide yes)
+			(effects (font (size 1.27 1.27)))
+		)
+		(pin "1"
+		)
+		(pin "2"
+		)
+		(instances
+			(project "LESHY2-RF"
+				(path "/58797fc0-4d05-5b8c-a153-b01d4ba46651"
+					(reference "C32043")
+					(unit 1)
+				)
+			)
+		)
+	)
+	(symbol
+		(lib_id "Leshy2:RF32_VOICE_EFUSE_EN_PULLUP")
+		(at 40.64 283.21 0)
+		(unit 1)
+		(exclude_from_sim no)
+		(in_bom yes)
+		(on_board yes)
+		(dnp no)
+		(property "Reference" "R32043"
+			(at 40.64 278.13 0)
+			(show_name no)
+			(do_not_autoplace no)
+			(effects (font (size 1.27 1.27)))
+		)
+		(property "Value" "Yageo RC0402FR-0710KL"
+			(at 40.64 288.29 0)
+			(show_name no)
+			(do_not_autoplace no)
+			(effects (font (size 1.27 1.27)))
+		)
+		(property "Footprint" "Resistor_SMD:R_0402_1005Metric"
+			(at 40.64 283.21 0)
+			(show_name no)
+			(do_not_autoplace no)
+			(hide yes)
+			(effects (font (size 1.27 1.27)))
+		)
+		(property "Datasheet" "~"
+			(at 40.64 283.21 0)
+			(show_name no)
+			(do_not_autoplace no)
+			(hide yes)
+			(effects (font (size 1.27 1.27)))
+		)
+		(property "Description" "10kohm_1pct_0402_main_feedback_bottom_resistor"
+			(at 40.64 283.21 0)
+			(show_name no)
+			(do_not_autoplace no)
+			(hide yes)
+			(effects (font (size 1.27 1.27)))
+		)
+		(pin "1"
+		)
+		(pin "2"
+		)
+		(instances
+			(project "LESHY2-RF"
+				(path "/58797fc0-4d05-5b8c-a153-b01d4ba46651"
+					(reference "R32043")
+					(unit 1)
+				)
+			)
 		)
 	)
@@
 		(effects (font (size 1.27 1.27)))
 	)
+	(label "AON_SAFE_3V3"
+		(at 337.82 279.40 180)
+		(effects (font (size 1.27 1.27)) (justify right bottom))
+	)
+	(label "AON_SAFE_3V3"
+		(at 190.50 279.40 0)
+		(effects (font (size 1.27 1.27)))
+	)
 	(hierarchical_label "AUDIO_GROUND"
 		(shape bidirectional)
@@
 		(effects (font (size 1.27 1.27)))
 	)
+	(hierarchical_label "CC_PWR_EN_PRIMARY"
+		(shape bidirectional)
+		(at 302.26 276.86 0)
+		(effects (font (size 1.27 1.27)))
+	)
 	(hierarchical_label "CC_PWR_EN_SAFE"
 		(shape bidirectional)
@@
 		(effects (font (size 1.27 1.27)))
 	)
+	(label "CC_PWR_EN_SAFE"
+		(at 337.82 276.86 180)
+		(effects (font (size 1.27 1.27)) (justify right bottom))
+	)
 	(label "CC_RBIAS"
 		(at 170.18 53.34 180)
@@
 		(effects (font (size 1.27 1.27)))
 	)
+	(hierarchical_label "FAULT_ASSERT_N"
+		(shape bidirectional)
+		(at 302.26 279.40 0)
+		(effects (font (size 1.27 1.27)))
+	)
 	(no_connect (at 226.06 45.72)
 	)
@@
 		(effects (font (size 1.27 1.27)) (justify right bottom))
 	)
+	(label "SAFETY_GROUND"
+		(at 302.26 281.94 0)
+		(effects (font (size 1.27 1.27)))
+	)
+	(label "SAFETY_GROUND"
+		(at 226.06 279.40 180)
+		(effects (font (size 1.27 1.27)) (justify right bottom))
+	)
 	(label "VOICE_4V_FB"
 		(at 337.82 233.68 180)
@@
 		(effects (font (size 1.27 1.27)))
 	)
+	(hierarchical_label "VOICE_EFUSE_BACKUP_EN_N"
+		(shape bidirectional)
+		(at 22.86 251.46 0)
+		(effects (font (size 1.27 1.27)))
+	)
+	(label "VOICE_EFUSE_BACKUP_EN_N"
+		(at 58.42 281.94 180)
+		(effects (font (size 1.27 1.27)) (justify right bottom))
+	)
 	(label "VOICE_EFUSE_DVDT"
 		(at 58.42 254.00 180)
@@
 	)
 	(label "VVOICE_RAW_4V"
-		(at 22.86 251.46 0)
-		(effects (font (size 1.27 1.27)))
-	)
-	(label "VVOICE_RAW_4V"
 		(at 22.86 261.62 0)
 		(effects (font (size 1.27 1.27)))
@@
 		(effects (font (size 1.27 1.27)))
 	)
+	(label "VVOICE_RAW_4V"
+		(at 22.86 281.94 0)
+		(effects (font (size 1.27 1.27)))
+	)
